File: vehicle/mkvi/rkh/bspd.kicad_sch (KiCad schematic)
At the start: 1 part

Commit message: Updates
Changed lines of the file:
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@@
 (kicad_sch (version 20211123) (generator eeschema)
   (paper "A4")
+  (hierarchical_label "SHDN_TO_BSPD" (shape input) (at 97.79 109.22 180)
+    (effects (font (size 1.27 1.27)) (justify right))
+  )
   (hierarchical_label "CAN{P M}" (shape bidirectional) (at 95.25 58.42 180)
     (effects (font (size 1.27 1.27)) (justify right))
   )
+  (hierarchical_label "SHDN_FROM_BSPD" (shape input) (at 93.7804 113.2295 180)
+    (effects (font (size 1.27 1.27)) (justify right))
+  )

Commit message: Continue adding connections
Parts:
- added SW601: SW_SPST, symbol Switch:SW_SPST
- gave numbers to parts that had none: 1
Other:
- note added: "In case BSPD doesn't work"
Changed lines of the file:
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@@
 (kicad_sch (version 20211123) (generator eeschema)
   (paper "A4")
+  (text "In case BSPD doesn't work" (at 215.9 77.47 0)
+    (effects (font (size 1.27 1.27)) (justify left bottom))
+  )
+  (hierarchical_label "BRAKE_PRESSURE_P" (shape output) (at 69.85 86.36 180)
+    (effects (font (size 1.27 1.27)) (justify right))
+  )
+  (hierarchical_label "BRAKE_PRESSURE_N" (shape output) (at 69.85 93.98 180)
+    (effects (font (size 1.27 1.27)) (justify right))
+  )
+  (hierarchical_label "BRAKE_PRESSURE_SENSE" (shape input) (at 76.2 90.17 0)
+    (effects (font (size 1.27 1.27)) (justify left))
+  )
   (hierarchical_label "SHDN_TO_BSPD" (shape input) (at 97.79 109.22 180)
     (effects (font (size 1.27 1.27)) (justify right))
@@
     (effects (font (size 1.27 1.27)) (justify left))
   )
+  (hierarchical_label "BRAKELIGHT_LSD" (shape output) (at 81.2624 101.5239 0)
+    (effects (font (size 1.27 1.27)) (justify left))
+  )
   (symbol (lib_id "formula:Automotive_M.2") (at 148.59 90.805 0) (unit 1)
     (in_bom yes) (on_board yes) (fields_autoplaced)
-    (property "Reference" "J?" (id 0) (at 148.59 41.91 0)
+    (property "Reference" "J601" (id 0) (at 148.59 41.91 0)
       (effects (font (size 1.778 1.5113)))
     )
@@
     (pin "P40")
   )
+  (symbol (lib_id "Switch:SW_SPST") (at 215.9 63.5 90) (unit 1)
+    (in_bom yes) (on_board yes) (fields_autoplaced)
+    (property "Reference" "SW601" (id 0) (at 217.17 62.2299 90)
+      (effects (font (size 1.27 1.27)) (justify right))
+    )
+    (property "Value" "SW_SPST" (id 1) (at 217.17 64.7699 90)
+      (effects (font (size 1.27 1.27)) (justify right))
+    )
+    (property "Footprint" "" (id 2) (at 215.9 63.5 0)
+      (effects (font (size 1.27 1.27)) hide)
+    )
+    (property "Datasheet" "~" (id 3) (at 215.9 63.5 0)
+      (effects (font (size 1.27 1.27)) hide)
+    )
+    (pin "1")
+    (pin "2")
+  )
 )

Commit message: --wip-- [skip ci]
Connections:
- net GND: now reaches J601.6
- net GND: now also J601.9
- net CAN.P: now reaches J601.7
- net CAN.M: now reaches J601.8
- no-connect marks 0 -> 2
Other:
- moved on the sheet: J601
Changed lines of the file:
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@@
 (kicad_sch (version 20211123) (generator eeschema)
   (paper "A4")
+  (no_connect (at 135.89 62.23))
+  (no_connect (at 135.89 59.69))
+  (bus_entry (at 124.46 72.39) (size 2.54 -2.54)
+    (stroke (width 0) (type default) (color 0 0 0 0))
+  )
+  (bus_entry (at 124.46 69.85) (size 2.54 -2.54)
+    (stroke (width 0) (type default) (color 0 0 0 0))
+  )
+  (bus (pts (xy 124.46 69.85) (xy 124.46 72.39))
+    (stroke (width 0) (type default) (color 0 0 0 0))
+  )
+  (wire (pts (xy 127 67.31) (xy 135.89 67.31))
+    (stroke (width 0) (type default) (color 0 0 0 0))
+  )
+  (wire (pts (xy 127 69.85) (xy 135.89 69.85))
+    (stroke (width 0) (type default) (color 0 0 0 0))
+  )
   (text "In case BSPD doesn't work" (at 215.9 77.47 0)
+    (effects (font (size 1.27 1.27)) (justify left bottom))
+  )
+  (label "GND" (at 135.89 72.39 180)
+    (effects (font (size 1.27 1.27)) (justify right bottom))
+  )
+  (label "GND" (at 135.89 64.77 180)
+    (effects (font (size 1.27 1.27)) (justify right bottom))
+  )
+  (label "CAN.P" (at 127 67.31 0)
+    (effects (font (size 1.27 1.27)) (justify left bottom))
+  )
+  (label "CAN.M" (at 127 69.85 0)
     (effects (font (size 1.27 1.27)) (justify left bottom))
   )
@@
     (effects (font (size 1.27 1.27)) (justify right))
   )
-  (hierarchical_label "CAN{P M}" (shape bidirectional) (at 95.25 58.42 180)
+  (hierarchical_label "CAN{P M}" (shape bidirectional) (at 124.46 72.39 180)
     (effects (font (size 1.27 1.27)) (justify right))
   )
-  (hierarchical_label "SHDN_FROM_BSPD" (shape input) (at 93.7804 113.2295 180)
+  (hierarchical_label "SHDN_FROM_BSPD" (shape input) (at 93.98 113.03 180)
     (effects (font (size 1.27 1.27)) (justify right))
   )
@@
     (effects (font (size 1.27 1.27)) (justify left))
   )
-  (hierarchical_label "BRAKELIGHT_LSD" (shape output) (at 81.2624 101.5239 0)
+  (hierarchical_label "BRAKELIGHT_LSD" (shape output) (at 81.28 101.6 0)
     (effects (font (size 1.27 1.27)) (justify left))
   )
-  (symbol (lib_id "formula:Automotive_M.2") (at 148.59 90.805 0) (unit 1)
+  (symbol (lib_id "formula:Automotive_M.2") (at 148.59 91.44 0) (unit 1)
     (in_bom yes) (on_board yes) (fields_autoplaced)
-    (property "Reference" "J601" (id 0) (at 148.59 41.91 0)
+    (property "Reference" "J601" (id 0) (at 148.59 42.545 0)
       (effects (font (size 1.778 1.5113)))
     )
-    (property "Value" "Automotive_M.2" (id 1) (at 148.59 45.72 0)
+    (property "Value" "Automotive_M.2" (id 1) (at 148.59 46.355 0)
       (effects (font (size 1.778 1.5113)))
     )
-    (property "Footprint" "footprints:Automotive_M.2" (id 2) (at 148.59 161.925 0)
+    (property "Footprint" "footprints:Automotive_M.2" (id 2) (at 148.59 162.56 0)
       (effects (font (size 1.27 1.27)) hide)
     )
-    (property "Datasheet" "" (id 3) (at 140.97 136.525 0)
+    (property "Datasheet" "" (id 3) (at 140.97 137.16 0)
       (effects (font (size 1.27 1.27)) hide)
     )

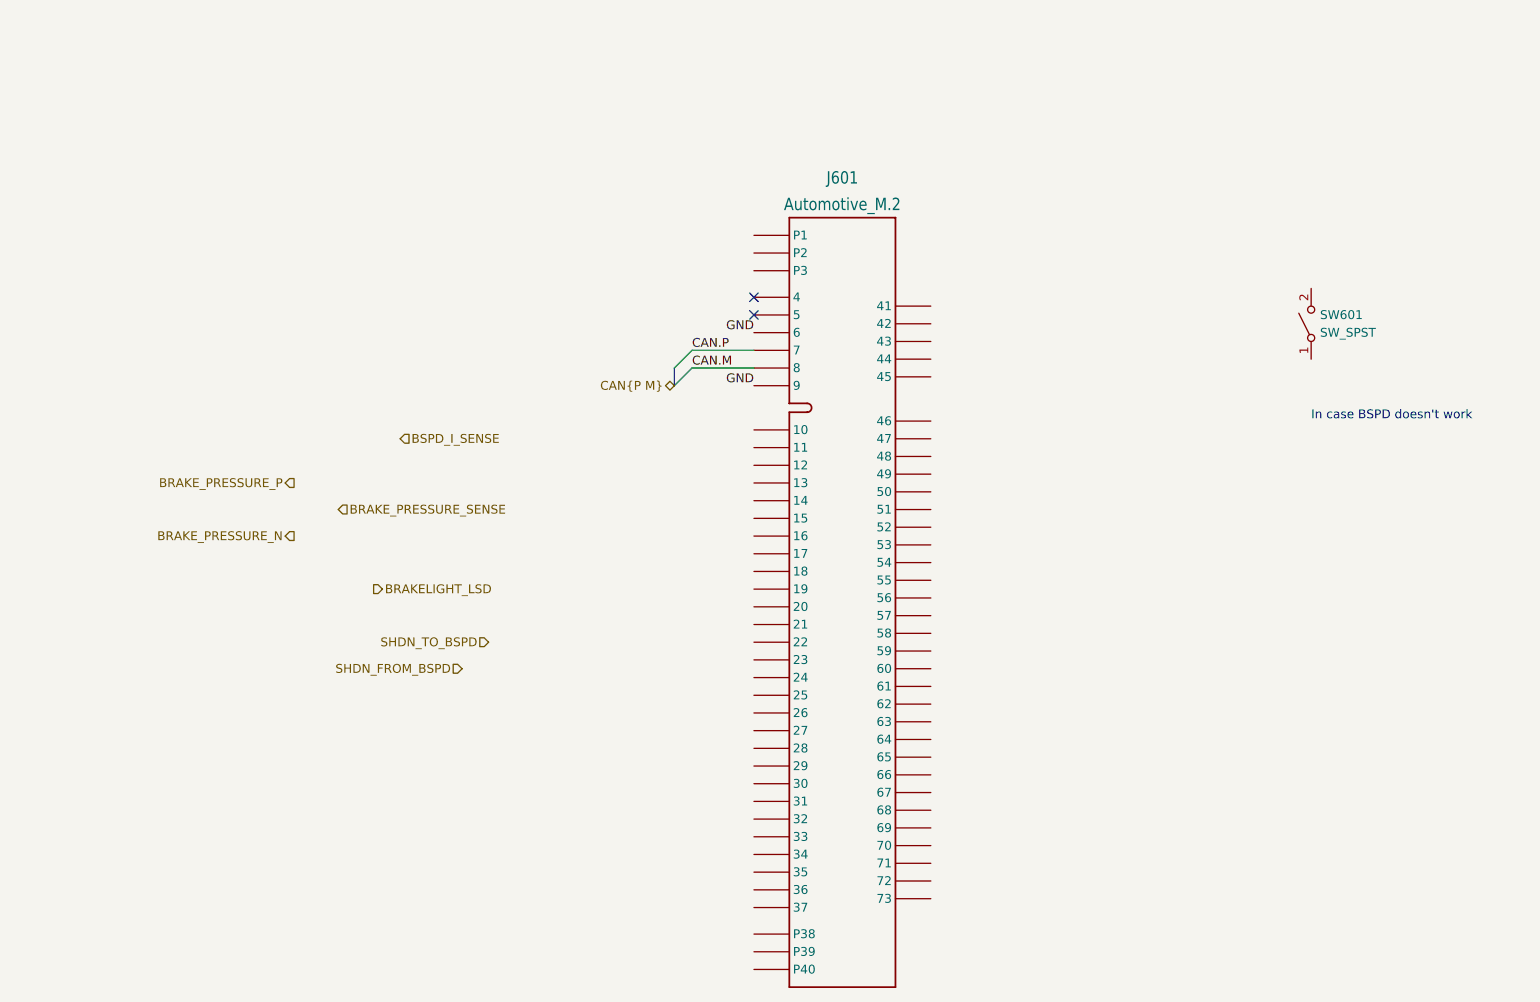
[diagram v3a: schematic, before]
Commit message: Add analog multiplexing
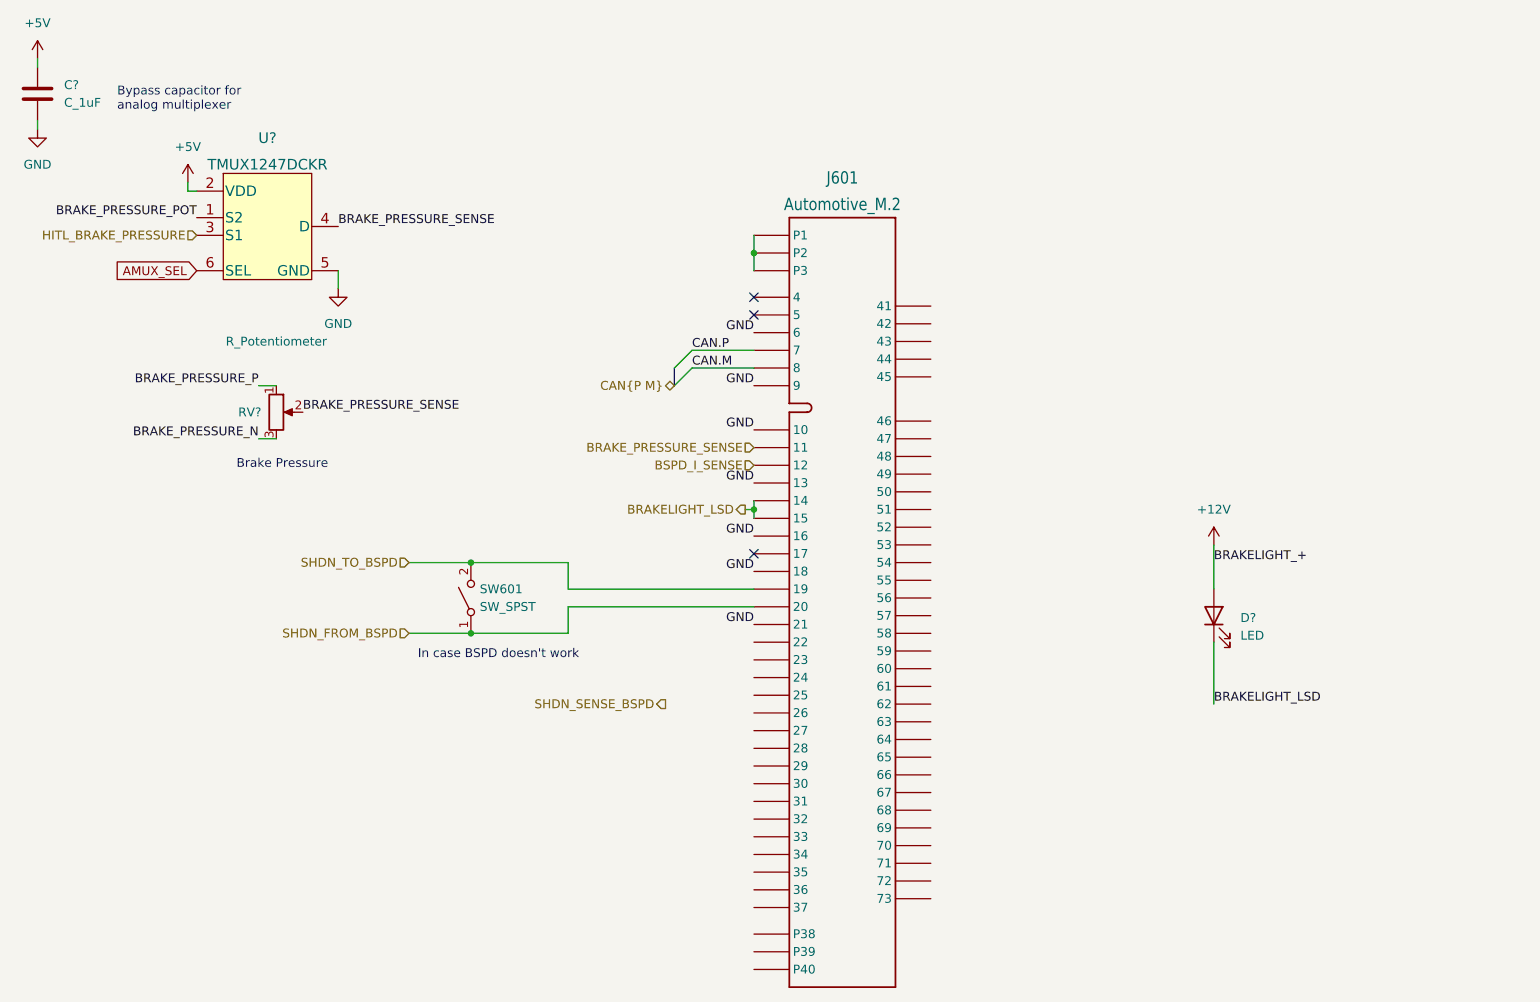
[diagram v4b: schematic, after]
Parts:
- added C?: C_1uF, footprints:C_0805_OEM, symbol formula:C_1uF
- added D?: LED, symbol Device:LED
- added RV?: R_Potentiometer, symbol Device:R_Potentiometer
- added U?: TMUX1247DCKR, SOT-SC70_DCK_6_TEX, symbol formula:TMUX1247DCKR
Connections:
- net BRAKELIGHT_LSD: now also J601.14, J601.15, D?.1 (K)
- net BRAKE_PRESSURE_N: now also RV?.3
- net BRAKE_PRESSURE_P: now also RV?.1
- net BRAKE_PRESSURE_SENSE: now also J601.11, RV?.2, U?.4 (D)
- net BSPD_I_SENSE: now also J601.12
- net GND: now also J601.10, J601.13, J601.16, J601.18, J601.21, C?.2, U?.5 (GND)
- net SHDN_FROM_BSPD: now also J601.20, SW601.1 (A)
- net SHDN_TO_BSPD: now also J601.19, SW601.2 (B)
- net at J601.P1: now also J601.P2, J601.P3
- new net +12V: D?.2 (A)
- new net +5V: C?.1, U?.2 (VDD)
- new net AMUX_SEL: U?.6 (SEL)
- new net BRAKE_PRESSURE_POT: U?.1 (S2)
- new net HITL_BRAKE_PRESSURE: U?.3 (S1)
- no-connect marks 2 -> 3
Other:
- note added: "Brake Pressure"
- note added: "Bypass capacitor for analog multiplexer"
- moved on the sheet: SW601

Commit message: Misc updates
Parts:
- added R601: R_1K, footprints:R_0805_OEM, symbol formula:R_1K
- gave numbers to parts that had none: 4
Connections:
- net +12V: now also R601.1; no longer D601.2 (A)
- net +5V: now also C601.2; no longer C601.1
- net GND: now also C601.1; no longer C601.2
- net SHDN_FROM_BSPD: no longer J601.20
- net SHDN_TO_BSPD: no longer J601.19
- new net: D601.2 (A), R601.2
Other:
- note removed: "Bypass capacitor for analog multiplexer"
- moved on the sheet: C601
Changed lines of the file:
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@@
   (junction (at 135.89 90.17) (diameter 0) (color 0 0 0 0)
+  )
+  (junction (at 54.61 41.91) (diameter 0) (color 0 0 0 0)
   )
   (no_connect (at 135.89 96.52))
@@
     (stroke (width 0) (type default) (color 0 0 0 0))
   )
-  (wire (pts (xy 109.22 104.14) (xy 135.89 104.14))
-    (stroke (width 0) (type default) (color 0 0 0 0))
-  )
-  (wire (pts (xy 54.61 43.18) (xy 54.61 44.45))
-    (stroke (width 0) (type default) (color 0 0 0 0))
-  )
-  (wire (pts (xy 135.89 101.6) (xy 109.22 101.6))
+  (wire (pts (xy 54.61 34.29) (xy 54.61 41.91))
     (stroke (width 0) (type default) (color 0 0 0 0))
   )
@@
     (stroke (width 0) (type default) (color 0 0 0 0))
   )
-  (wire (pts (xy 33.02 34.29) (xy 33.02 35.56))
-    (stroke (width 0) (type default) (color 0 0 0 0))
-  )
   (wire (pts (xy 201.93 109.22) (xy 201.93 118.11))
     (stroke (width 0) (type default) (color 0 0 0 0))
@@
     (stroke (width 0) (type default) (color 0 0 0 0))
   )
-  (wire (pts (xy 33.02 25.4) (xy 33.02 26.67))
+  (wire (pts (xy 54.61 41.91) (xy 54.61 44.45))
+    (stroke (width 0) (type default) (color 0 0 0 0))
+  )
+  (wire (pts (xy 201.93 99.06) (xy 201.93 101.6))
     (stroke (width 0) (type default) (color 0 0 0 0))
   )
@@
     (stroke (width 0) (type default) (color 0 0 0 0))
   )
-  (wire (pts (xy 201.93 95.25) (xy 201.93 101.6))
+  (wire (pts (xy 201.93 87.63) (xy 201.93 91.44))
+    (stroke (width 0) (type default) (color 0 0 0 0))
+  )
+  (wire (pts (xy 45.72 41.91) (xy 46.99 41.91))
     (stroke (width 0) (type default) (color 0 0 0 0))
   )
@@
     (effects (font (size 1.27 1.27)) (justify left bottom))
   )
-  (text "Bypass capacitor for\nanalog multiplexer" (at 44.45 33.02 0)
-    (effects (font (size 1.27 1.27)) (justify left bottom))
-  )
   (text "In case BSPD doesn't work" (at 87.63 111.76 0)
     (effects (font (size 1.27 1.27)) (justify left bottom))
@@
     (effects (font (size 1.27 1.27)) (justify left bottom))
   )
-  (label "BRAKELIGHT_+" (at 201.93 97.79 0)
+  (label "GND" (at 45.72 41.91 180)
+    (effects (font (size 1.27 1.27)) (justify right bottom))
+  )
+  (label "BRAKELIGHT_+" (at 201.93 90.17 0)
     (effects (font (size 1.27 1.27)) (justify left bottom))
   )
@@
     (effects (font (size 1.27 1.27)) (justify right))
   )
-  (symbol (lib_id "power:+12V") (at 201.93 95.25 0) (unit 1)
-    (in_bom yes) (on_board yes) (fields_autoplaced)
-    (property "Reference" "#PWR?" (id 0) (at 201.93 99.06 0)
-      (effects (font (size 1.27 1.27)) hide)
-    )
-    (property "Value" "+12V" (id 1) (at 201.93 90.17 0))
-    (property "Footprint" "" (id 2) (at 201.93 95.25 0)
-      (effects (font (size 1.27 1.27)) hide)
-    )
-    (property "Datasheet" "" (id 3) (at 201.93 95.25 0)
+  (symbol (lib_id "power:+12V") (at 201.93 87.63 0) (unit 1)
+    (in_bom yes) (on_board yes) (fields_autoplaced)
+    (property "Reference" "#PWR?" (id 0) (at 201.93 91.44 0)
+      (effects (font (size 1.27 1.27)) hide)
+    )
+    (property "Value" "+12V" (id 1) (at 201.93 82.55 0))
+    (property "Footprint" "" (id 2) (at 201.93 87.63 0)
+      (effects (font (size 1.27 1.27)) hide)
+    )
+    (property "Datasheet" "" (id 3) (at 201.93 87.63 0)
       (effects (font (size 1.27 1.27)) hide)
     )
@@
     (pin "P40")
   )
-  (symbol (lib_id "power:+5V") (at 33.02 25.4 0) (unit 1)
-    (in_bom yes) (on_board yes) (fields_autoplaced)
-    (property "Reference" "#PWR?" (id 0) (at 33.02 29.21 0)
-      (effects (font (size 1.27 1.27)) hide)
-    )
-    (property "Value" "+5V" (id 1) (at 33.02 20.32 0))
-    (property "Footprint" "" (id 2) (at 33.02 25.4 0)
-      (effects (font (size 1.27 1.27)) hide)
-    )
-    (property "Datasheet" "" (id 3) (at 33.02 25.4 0)
-      (effects (font (size 1.27 1.27)) hide)
-    )
-    (pin "1")
-  )
-  (symbol (lib_id "formula:C_1uF") (at 33.02 31.75 0) (unit 1)
-    (in_bom yes) (on_board yes) (fields_autoplaced)
-    (property "Reference" "C?" (id 0) (at 36.83 29.2099 0)
+  (symbol (lib_id "formula:C_1uF") (at 52.07 41.91 90) (unit 1)
+    (in_bom yes) (on_board yes)
+    (property "Reference" "C601" (id 0) (at 53.34 38.1 90)
       (effects (font (size 1.27 1.27)) (justify left))
     )
-    (property "Value" "C_1uF" (id 1) (at 36.83 31.7499 0)
+    (property "Value" "C_1uF" (id 1) (at 53.34 35.56 90)
       (effects (font (size 1.27 1.27)) (justify left))
     )
-    (property "Footprint" "footprints:C_0805_OEM" (id 2) (at 33.9852 16.51 0)
-      (effects (font (size 1.27 1.27)) hide)
-    )
-    (property "Datasheet" "https://media.digikey.com/pdf/Data%20Sheets/Samsung%20PDFs/CL21B105KBFNNNG_Spec.pdf" (id 3) (at 33.655 10.16 0)
-      (effects (font (size 1.27 1.27)) hide)
-    )
-    (property "PurchasingLink" "https://www.digikey.com/en/products/detail/samsung-electro-mechanics/CL21B105KBFNNNG/3894467" (id 4) (at 43.815 19.05 0)
-      (effects (font (size 1.524 1.524)) hide)
-    )
-    (property "MFN" "DK" (id 5) (at 33.02 31.75 0)
-      (effects (font (size 1.27 1.27)) hide)
-    )
-    (property "MPN" "1276-6470-1-ND" (id 6) (at 33.02 31.75 0)
+    (property "Footprint" "footprints:C_0805_OEM" (id 2) (at 36.83 40.9448 0)
+      (effects (font (size 1.27 1.27)) hide)
+    )
+    (property "Datasheet" "https://media.digikey.com/pdf/Data%20Sheets/Samsung%20PDFs/CL21B105KBFNNNG_Spec.pdf" (id 3) (at 30.48 41.275 0)
+      (effects (font (size 1.27 1.27)) hide)
+    )
+    (property "PurchasingLink" "https://www.digikey.com/en/products/detail/samsung-electro-mechanics/CL21B105KBFNNNG/3894467" (id 4) (at 39.37 31.115 0)
+      (effects (font (size 1.524 1.524)) hide)
+    )
+    (property "MFN" "DK" (id 5) (at 52.07 41.91 0)
+      (effects (font (size 1.27 1.27)) hide)
+    )
+    (property "MPN" "1276-6470-1-ND" (id 6) (at 52.07 41.91 0)
       (effects (font (size 1.27 1.27)) hide)
     )
@@
     (pin "2")
   )
+  (symbol (lib_id "formula:R_1K") (at 201.93 95.25 0) (unit 1)
+    (in_bom yes) (on_board yes) (fields_autoplaced)
+    (property "Reference" "R601" (id 0) (at 204.47 93.9799 0)
+      (effects (font (size 1.27 1.27)) (justify left))
+    )
+    (property "Value" "R_1K" (id 1) (at 204.47 96.5199 0)
+      (effects (font (size 1.27 1.27)) (justify left))
+    )
+    (property "Footprint" "footprints:R_0805_OEM" (id 2) (at 200.152 95.25 0)
+      (effects (font (size 1.27 1.27)) hide)
+    )
+    (property "Datasheet" "https://www.seielect.com/Catalog/SEI-rncp.pdf" (id 3) (at 203.962 95.25 0)
+      (effects (font (size 1.27 1.27)) hide)
+    )
+    (property "MFN" "DK" (id 4) (at 201.93 95.25 0)
+      (effects (font (size 1.524 1.524)) hide)
+    )
+    (property "MPN" "RNCP0805FTD1K00CT-ND" (id 5) (at 201.93 95.25 0)
+      (effects (font (size 1.524 1.524)) hide)
+    )
+    (property "PurchasingLink" "https://www.digikey.com/products/en?keywords=RNCP0805FTD1K00CT-ND" (id 6) (at 214.122 85.09 0)
+      (effects (font (size 1.524 1.524)) hide)
+    )
+    (pin "1")
+    (pin "2")
+  )
   (symbol (lib_id "Device:LED") (at 201.93 105.41 90) (unit 1)
     (in_bom yes) (on_board yes) (fields_autoplaced)
-    (property "Reference" "D?" (id 0) (at 205.74 105.7274 90)
+    (property "Reference" "D601" (id 0) (at 205.74 105.7274 90)
       (effects (font (size 1.27 1.27)) (justify right))
     )
@@
   (symbol (lib_id "formula:TMUX1247DCKR") (at 66.04 49.53 0) (unit 1)
     (in_bom yes) (on_board yes) (fields_autoplaced)
-    (property "Reference" "U?" (id 0) (at 66.04 36.83 0)
+    (property "Reference" "U601" (id 0) (at 66.04 36.83 0)
       (effects (font (size 1.524 1.524)))
     )
@@
     (pin "6")
   )
-  (symbol (lib_id "power:GND") (at 33.02 35.56 0) (unit 1)
-    (in_bom yes) (on_board yes) (fields_autoplaced)
-    (property "Reference" "#PWR?" (id 0) (at 33.02 41.91 0)
-      (effects (font (size 1.27 1.27)) hide)
-    )
-    (property "Value" "GND" (id 1) (at 33.02 40.64 0))
-    (property "Footprint" "" (id 2) (at 33.02 35.56 0)
-      (effects (font (size 1.27 1.27)) hide)
-    )
-    (property "Datasheet" "" (id 3) (at 33.02 35.56 0)
-      (effects (font (size 1.27 1.27)) hide)
-    )
-    (pin "1")
-  )
-  (symbol (lib_id "power:+5V") (at 54.61 43.18 0) (unit 1)
-    (in_bom yes) (on_board yes) (fields_autoplaced)
-    (property "Reference" "#PWR?" (id 0) (at 54.61 46.99 0)
-      (effects (font (size 1.27 1.27)) hide)
-    )
-    (property "Value" "+5V" (id 1) (at 54.61 38.1 0))
-    (property "Footprint" "" (id 2) (at 54.61 43.18 0)
-      (effects (font (size 1.27 1.27)) hide)
-    )
-    (property "Datasheet" "" (id 3) (at 54.61 43.18 0)
+  (symbol (lib_id "power:+5V") (at 54.61 34.29 0) (unit 1)
+    (in_bom yes) (on_board yes) (fields_autoplaced)
+    (property "Reference" "#PWR?" (id 0) (at 54.61 38.1 0)
+      (effects (font (size 1.27 1.27)) hide)
+    )
+    (property "Value" "+5V" (id 1) (at 54.61 29.21 0))
+    (property "Footprint" "" (id 2) (at 54.61 34.29 0)
+      (effects (font (size 1.27 1.27)) hide)
+    )
+    (property "Datasheet" "" (id 3) (at 54.61 34.29 0)
       (effects (font (size 1.27 1.27)) hide)
     )
@@
   (symbol (lib_id "Device:R_Potentiometer") (at 67.31 76.2 0) (unit 1)
     (in_bom yes) (on_board yes)
-    (property "Reference" "RV?" (id 0) (at 63.5 76.2 0))
+    (property "Reference" "RV601" (id 0) (at 63.5 76.2 0))
     (property "Value" "R_Potentiometer" (id 1) (at 67.31 66.04 0))
     (property "Footprint" "" (id 2) (at 67.31 76.2 0)
